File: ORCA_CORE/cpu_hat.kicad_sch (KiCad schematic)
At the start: 0 parts

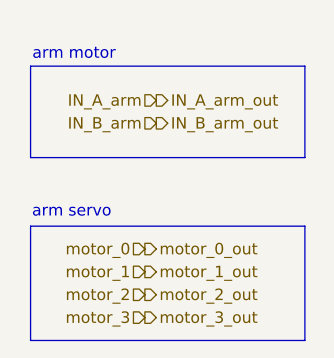
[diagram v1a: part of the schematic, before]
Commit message: add power registers to power_board gate driver
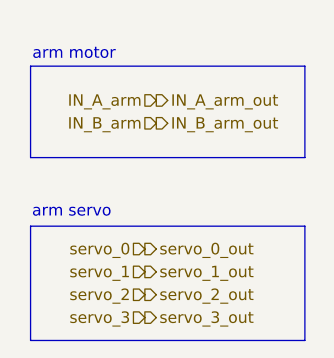
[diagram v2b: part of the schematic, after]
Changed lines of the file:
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@@
-		)
-	)
-	(hierarchical_label "motor_2"
-		(shape input)
-		(at 40.64 93.98 180)
-		(fields_autoplaced yes)
-		(effects
-			(font
-				(size 1.27 1.27)
-			)
-			(justify right)
 		)
 	)
@@
 		)
 	)
-	(hierarchical_label "motor_1"
-		(shape input)
-		(at 40.64 91.44 180)
-		(fields_autoplaced yes)
-		(effects
-			(font
-				(size 1.27 1.27)
-			)
-			(justify right)
-		)
-	)
-	(hierarchical_label "motor_2_out"
-		(shape output)
-		(at 40.64 93.98 0)
-		(fields_autoplaced yes)
-		(effects
-			(font
-				(size 1.27 1.27)
-			)
-			(justify left)
-		)
-	)
 	(hierarchical_label "IN_B_fork"
 		(shape input)
@@
 		)
 	)
-	(hierarchical_label "motor_0"
+	(hierarchical_label "servo_0"
 		(shape input)
 		(at 40.64 88.9 180)
@@
 		)
 	)
-	(hierarchical_label "motor_1_out"
+	(hierarchical_label "servo_1_out"
 		(shape output)
 		(at 40.64 91.44 0)
@@
 		)
 	)
-	(hierarchical_label "motor_3_out"
+	(hierarchical_label "servo_3_out"
 		(shape output)
 		(at 40.64 96.52 0)
@@
 			)
 			(justify left)
+		)
+	)
+	(hierarchical_label "servo_1"
+		(shape input)
+		(at 40.64 91.44 180)
+		(fields_autoplaced yes)
+		(effects
+			(font
+				(size 1.27 1.27)
+			)
+			(justify right)
+		)
+	)
+	(hierarchical_label "servo_2"
+		(shape input)
+		(at 40.64 93.98 180)
+		(fields_autoplaced yes)
+		(effects
+			(font
+				(size 1.27 1.27)
+			)
+			(justify right)
 		)
 	)
@@
 		)
 	)
-	(hierarchical_label "motor_3"
-		(shape input)
-		(at 40.64 96.52 180)
+	(hierarchical_label "servo_2_out"
+		(shape output)
+		(at 40.64 93.98 0)
 		(fields_autoplaced yes)
 		(effects
@@
 				(size 1.27 1.27)
 			)
-			(justify right)
+			(justify left)
 		)
 	)
@@
 		)
 	)
-	(hierarchical_label "motor_0_out"
+	(hierarchical_label "servo_3"
+		(shape input)
+		(at 40.64 96.52 180)
+		(fields_autoplaced yes)
+		(effects
+			(font
+				(size 1.27 1.27)
+			)
+			(justify right)
+		)
+	)
+	(hierarchical_label "servo_0_out"
 		(shape output)
 		(at 40.64 88.9 0)

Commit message: almost completed CORE
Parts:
- added J17: data_line_power, Connector_JST:JST_XH_B3B-XH-A_1x03_P2.50mm_Vertical, symbol Connector_Generic:Conn_01x03
- added J31: I2C_1, Connector_JST:JST_XH_B3B-XH-A_1x03_P2.50mm_Vertical, symbol Connector_Generic:Conn_01x03
- added J32: I2C_2, Connector_JST:JST_XH_B3B-XH-A_1x03_P2.50mm_Vertical, symbol Connector_Generic:Conn_01x03
- added R37, R38, R57, R58: 2.2k, symbol Device:R
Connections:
- new net +3V3_cpu: J31.1 (Pin_1), J32.1 (Pin_1), R37.1, R38.1, R57.1, R58.1
- new net SCL: J31.2 (Pin_2), J32.2 (Pin_2), R38.2, R58.2
- new net SDA: J31.3 (Pin_3), J32.3 (Pin_3), R37.2, R57.2
- new net emerge_detector: J17.1 (Pin_1)
- new net emerge_order: J17.3 (Pin_3)
- new net power_checker: J17.2 (Pin_2)
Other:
- note added: "camera"
- note added: "data line"
- note added: "full color led"
- note added: "i2c"
- note added: "reset"
- note added: "uart"

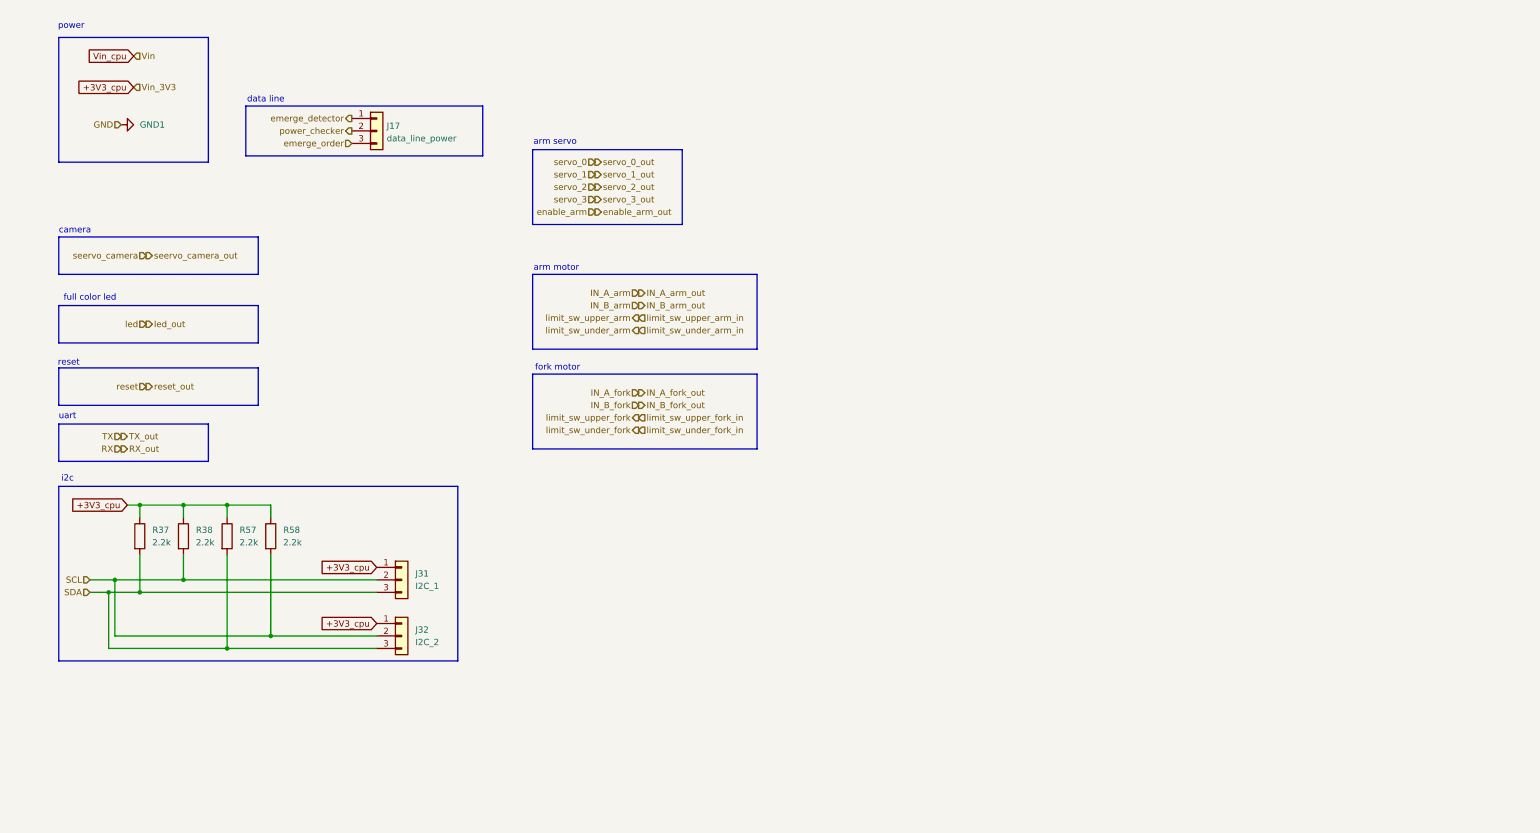
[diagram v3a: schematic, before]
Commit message: complete attaching footprint of CORE
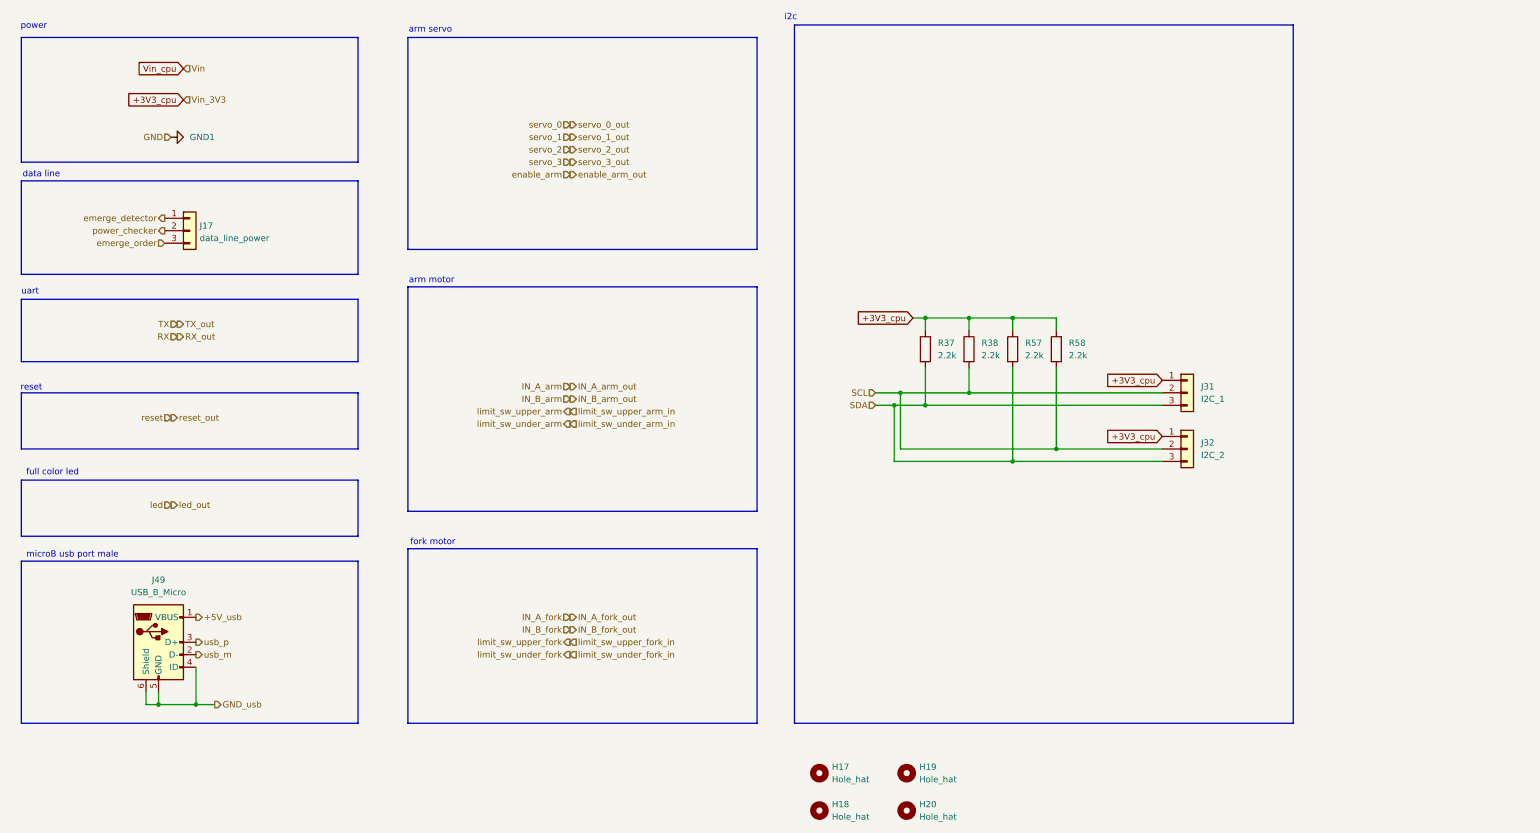
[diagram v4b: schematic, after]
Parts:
- added H17, H18, H19, H20: Hole_hat, MountingHole:MountingHole_3.2mm_M3, symbol Mechanical:MountingHole
- added J49: USB_B_Micro, digikey-footprints:USB_Micro_B_Male_UJ2-MIBH-4-SMT-TR, symbol Connector:USB_B_Micro
- R37, R38, R57, R58: footprint (none) -> Resistor_SMD:R_0603_1608Metric_Pad0.98x0.95mm_HandSolder
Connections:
- new net +5V_usb: J49.1 (VBUS)
- new net GND_usb: J49.4 (ID), J49.5 (GND), J49.6 (Shield)
- new net usb_m: J49.2 (D-)
- new net usb_p: J49.3 (D+)
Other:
- note added: "microB usb port male"
- note removed: "camera"
- moved on the sheet: J17, J31, J32, R37, R38, R57, R58

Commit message: place most of footprints. test replicate
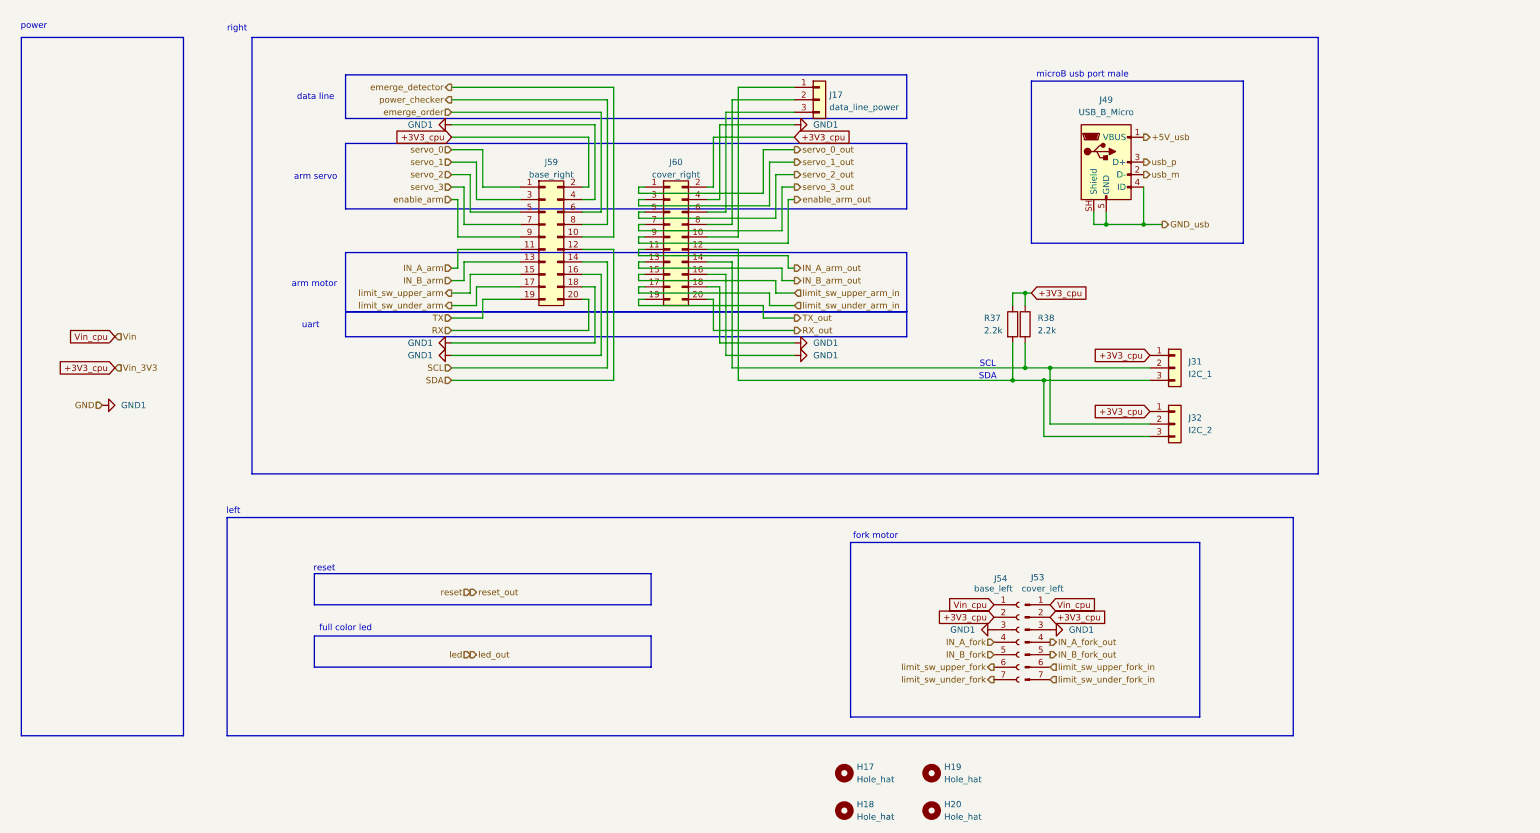
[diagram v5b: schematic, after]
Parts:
- removed R57, R58: 2.2k, Resistor_SMD:R_0603_1608Metric_Pad0.98x0.95mm_HandSolder, symbol Device:R
- added J53: cover_left, Connector_PinHeader_2.54mm:PinHeader_1x07_P2.54mm_Vertical, symbol Connector:Conn_01x07_Pin
- added J54: base_left, Connector_PinSocket_2.54mm:PinSocket_1x07_P2.54mm_Vertical, symbol Connector:Conn_01x07_Socket
- added J59: base_right, Connector_PinSocket_2.54mm:PinSocket_2x10_P2.54mm_Vertical, symbol Connector_Generic:Conn_02x10_Odd_Even
- added J60: cover_right, Connector_PinHeader_2.54mm:PinHeader_2x10_P2.54mm_Vertical, symbol Connector_Generic:Conn_02x10_Odd_Even
- J49: footprint digikey-footprints:USB_Micro_B_Male_UJ2-MIBH-4-SMT-TR -> Conn:ZX60-B-5S(31)
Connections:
- net +3V3_cpu: now also J53.2 (Pin_2), J54.2 (Pin_2), J59.2 (Pin_2), J60.2 (Pin_2)
- net GND1: now also J53.3 (Pin_3), J54.3 (Pin_3), J59.16 (Pin_16), J59.18 (Pin_18), J59.4 (Pin_4), J60.16 (Pin_16), J60.18 (Pin_18), J60.4 (Pin_4)
- net GND_usb: now also J49.SH (Shield); no longer J49.6 (Shield)
- net IN_A_arm: now also J59.11 (Pin_11)
- net IN_A_fork: now also J54.4 (Pin_4)
- net IN_B_arm: now also J59.13 (Pin_13)
- net IN_B_fork: now also J54.5 (Pin_5)
- net RX: now also J59.20 (Pin_20)
- net SCL: now also J59.14 (Pin_14); no longer J31.2 (Pin_2), J32.2 (Pin_2), R38.2
- net SDA: now also J59.12 (Pin_12); no longer J31.3 (Pin_3), J32.3 (Pin_3), R37.2
- net TX: now also J59.19 (Pin_19)
- net Vin_cpu: now also J53.1 (Pin_1), J54.1 (Pin_1)
- net emerge_detector: now also J59.10 (Pin_10); no longer J17.1 (Pin_1)
- net emerge_order: now also J59.6 (Pin_6); no longer J17.3 (Pin_3)
- net enable_arm: now also J59.9 (Pin_9)
- net limit_sw_under_arm: now also J59.17 (Pin_17)
- net limit_sw_under_fork: now also J54.7 (Pin_7)
- net limit_sw_upper_arm: now also J59.15 (Pin_15)
- net limit_sw_upper_fork: now also J54.6 (Pin_6)
- net power_checker: now also J59.8 (Pin_8); no longer J17.2 (Pin_2)
- net servo_0: now also J59.1 (Pin_1)
- net servo_1: now also J59.3 (Pin_3)
- net servo_2: now also J59.5 (Pin_5)
- net servo_3: now also J59.7 (Pin_7)
- new net: J31.2 (Pin_2), J32.2 (Pin_2), J60.14 (Pin_14), R38.2
- new net: J17.1 (Pin_1), J60.10 (Pin_10)
- new net: J17.2 (Pin_2), J60.8 (Pin_8)
- new net: J17.3 (Pin_3), J60.6 (Pin_6)
- new net: J31.3 (Pin_3), J32.3 (Pin_3), J60.12 (Pin_12), R37.2
- new net IN_A_arm_out: J60.11 (Pin_11)
- new net IN_A_fork_out: J53.4 (Pin_4)
- new net IN_B_arm_out: J60.13 (Pin_13)
- new net IN_B_fork_out: J53.5 (Pin_5)
- new net RX_out: J60.20 (Pin_20)
- new net TX_out: J60.19 (Pin_19)
- new net enable_arm_out: J60.9 (Pin_9)
- new net limit_sw_under_arm_in: J60.17 (Pin_17)
- new net limit_sw_under_fork_in: J53.7 (Pin_7)
- new net limit_sw_upper_arm_in: J60.15 (Pin_15)
- new net limit_sw_upper_fork_in: J53.6 (Pin_6)
- new net servo_0_out: J60.1 (Pin_1)
- new net servo_1_out: J60.3 (Pin_3)
- new net servo_2_out: J60.5 (Pin_5)
- new net servo_3_out: J60.7 (Pin_7)
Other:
- note added: "SCL"
- note added: "SDA"
- note added: "left"
- note added: "right"
- note removed: "i2c"
- moved on the sheet: H17, H18, H19, H20, J17, J31, J32, J49, R37, R38

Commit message: most of wire placed. try update kicad to use replicate library
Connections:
- net +3V3_cpu: no longer J31.1 (Pin_1), J32.1 (Pin_1), J53.2 (Pin_2), J54.2 (Pin_2), J59.2 (Pin_2), J60.2 (Pin_2)
- net GND1: no longer J59.16 (Pin_16), J60.16 (Pin_16)
- net Vin_cpu renamed Vin_cpu_hat
- net Vin_cpu_hat: now also J59.16 (Pin_16), J60.16 (Pin_16)
- new net +3V3_cpu_hat: J31.1 (Pin_1), J32.1 (Pin_1), J53.2 (Pin_2), J54.2 (Pin_2), J59.2 (Pin_2), J60.2 (Pin_2)
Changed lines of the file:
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@@
 		)
 	)
-	(global_label "Vin_cpu"
+	(global_label "Vin_cpu_hat"
 		(shape input)
 		(at 39.37 81.28 180)
@@
 		)
 		(property "Intersheetrefs" "${INTERSHEET_REFS}"
-			(at 29.1882 81.28 0)
+			(at 25.1969 81.28 0)
 			(effects
 				(font
@@
 		)
 	)
-	(global_label "+3V3_cpu"
+	(global_label "+3V3_cpu_hat"
 		(shape input)
 		(at 177.8 40.64 0)
@@
 		)
 		(property "Intersheetrefs" "${INTERSHEET_REFS}"
-			(at 190.2194 40.64 0)
+			(at 194.2107 40.64 0)
 			(effects
 				(font
@@
 		)
 	)
-	(global_label "+3V3_cpu"
+	(global_label "Vin_cpu_hat"
+		(shape input)
+		(at 177.8 85.09 0)
+		(fields_autoplaced yes)
+		(effects
+			(font
+				(size 1.27 1.27)
+			)
+			(justify left)
+		)
+		(property "Intersheetrefs" "${INTERSHEET_REFS}"
+			(at 191.9731 85.09 0)
+			(effects
+				(font
+					(size 1.27 1.27)
+				)
+				(justify left)
+				(hide yes)
+			)
+		)
+	)
+	(global_label "+3V3_cpu_hat"
 		(shape input)
 		(at 250.19 85.09 180)
@@
 		)
 		(property "Intersheetrefs" "${INTERSHEET_REFS}"
-			(at 237.7706 85.09 0)
+			(at 233.7793 85.09 0)
 			(effects
 				(font
@@
 		)
 	)
-	(global_label "Vin_cpu"
+	(global_label "Vin_cpu_hat"
 		(shape input)
 		(at 229.87 135.89 0)
@@
 		)
 		(property "Intersheetrefs" "${INTERSHEET_REFS}"
-			(at 240.0518 135.89 0)
+			(at 244.0431 135.89 0)
 			(effects
 				(font
@@
 		)
 	)
-	(global_label "Vin_cpu"
+	(global_label "Vin_cpu_hat"
 		(shape input)
 		(at 218.44 135.89 180)
@@
 		)
 		(property "Intersheetrefs" "${INTERSHEET_REFS}"
-			(at 208.2582 135.89 0)
+			(at 204.2669 135.89 0)
 			(effects
 				(font
@@
 		)
 	)
-	(global_label "+3V3_cpu"
+	(global_label "Vin_cpu_hat"
+		(shape input)
+		(at 107.95 85.09 180)
+		(fields_autoplaced yes)
+		(effects
+			(font
+				(size 1.27 1.27)
+			)
+			(justify right)
+		)
+		(property "Intersheetrefs" "${INTERSHEET_REFS}"
+			(at 93.7769 85.09 0)
+			(effects
+				(font
+					(size 1.27 1.27)
+				)
+				(justify right)
+				(hide yes)
+			)
+		)
+	)
+	(global_label "+3V3_cpu_hat"
 		(shape input)
 		(at 39.37 87.63 180)
@@
 		)
 		(property "Intersheetrefs" "${INTERSHEET_REFS}"
-			(at 26.9506 87.63 0)
+			(at 22.9593 87.63 0)
 			(effects
 				(font
@@
 		)
 	)
-	(global_label "+3V3_cpu"
+	(global_label "+3V3_cpu_hat"
 		(shape input)
 		(at 218.44 138.43 180)
@@
 		)
 		(property "Intersheetrefs" "${INTERSHEET_REFS}"
-			(at 206.0206 138.43 0)
+			(at 202.0293 138.43 0)
 			(effects
 				(font
@@
 		)
 	)
-	(global_label "+3V3_cpu"
+	(global_label "+3V3_cpu_hat"
 		(shape input)
 		(at 107.95 40.64 180)
@@
 		)
 		(property "Intersheetrefs" "${INTERSHEET_REFS}"
-			(at 95.5306 40.64 0)
+			(at 91.5393 40.64 0)
 			(effects
 				(font
@@
 		)
 	)
-	(global_label "+3V3_cpu"
+	(global_label "+3V3_cpu_hat"
 		(shape input)
 		(at 229.87 138.43 0)
@@
 		)
 		(property "Intersheetrefs" "${INTERSHEET_REFS}"
-			(at 242.2894 138.43 0)
+			(at 246.2807 138.43 0)
 			(effects
 				(font
@@
 		)
 	)
-	(global_label "+3V3_cpu"
+	(global_label "+3V3_cpu_hat"
 		(shape input)
 		(at 250.19 96.52 180)
@@
 		)
 		(property "Intersheetrefs" "${INTERSHEET_REFS}"
-			(at 237.7706 96.52 0)
+			(at 233.7793 96.52 0)
 			(effects
 				(font
@@
 			)
 			(justify left)
-		)
-	)
-	(symbol
-		(lib_id "power:GND1")
-		(at 107.95 85.09 270)
-		(unit 1)
-		(exclude_from_sim no)
-		(in_bom yes)
-		(on_board yes)
-		(dnp no)
-		(fields_autoplaced yes)
-		(property "Reference" "#PWR0130"
-			(at 101.6 85.09 0)
-			(effects
-				(font
-					(size 1.27 1.27)
-				)
-				(hide yes)
-			)
-		)
-		(property "Value" "GND1"
-			(at 104.14 85.0899 90)
-			(effects
-				(font
-					(size 1.27 1.27)
-				)
-				(justify right)
-			)
-		)
-		(property "Footprint" ""
-			(at 107.95 85.09 0)
-			(effects
-				(font
-					(size 1.27 1.27)
-				)
-				(hide yes)
-			)
-		)
-		(property "Datasheet" ""
-			(at 107.95 85.09 0)
-			(effects
-				(font
-					(size 1.27 1.27)
-				)
-				(hide yes)
-			)
-		)
-		(property "Description" "Power symbol creates a global label with name \"GND1\" , ground"
-			(at 107.95 85.09 0)
-			(effects
-				(font
-					(size 1.27 1.27)
-				)
-				(hide yes)
-			)
-		)
-		(pin "1"
-		)
-		(instances
-			(project "ORCA_CORE"
-				(path "/895d6bb7-4008-488b-a34b-0077e9f7e4a1/663b2318-8aea-45e9-89db-8c327bbfd340"
-					(reference "#PWR0130")
-					(unit 1)
-				)
-			)
 		)
 	)
@@
 					(unit 1)
 				)
-			)
-		)
-	)
-	(symbol
-		(lib_id "power:GND1")
-		(at 177.8 85.09 90)
-		(unit 1)
-		(exclude_from_sim no)
-		(in_bom yes)
-		(on_board yes)
-		(dnp no)
-		(fields_autoplaced yes)
-		(property "Reference" "#PWR0131"
-			(at 184.15 85.09 0)
-			(effects
-				(font
-					(size 1.27 1.27)
-				)
-				(hide yes)
-			)
-		)
-		(property "Value" "GND1"
-			(at 181.61 85.0899 90)
-			(effects
-				(font
-					(size 1.27 1.27)
-				)
-				(justify right)
-			)
-		)
-		(property "Footprint" ""
-			(at 177.8 85.09 0)
-			(effects
-				(font
-					(size 1.27 1.27)
-				)
-				(hide yes)
-			)
-		)
-		(property "Datasheet" ""
-			(at 177.8 85.09 0)
-			(effects
-				(font
-					(size 1.27 1.27)
-				)
-				(hide yes)
-			)
-		)
-		(property "Description" "Power symbol creates a global label with name \"GND1\" , ground"
-			(at 177.8 85.09 0)
-			(effects
-				(font
-					(size 1.27 1.27)
-				)
-				(hide yes)
-			)
-		)
-		(pin "1"
-		)
-		(instances
-			(project "ORCA_CORE"
-				(path "/895d6bb7-4008-488b-a34b-0077e9f7e4a1/663b2318-8aea-45e9-89db-8c327bbfd340"
-					(reference "#PWR0131")
-					(unit 1)
-				)
